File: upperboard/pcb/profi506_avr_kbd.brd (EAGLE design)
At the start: 22.8 x 53 mm, 15 parts, among them IC1 ATMEGA328-QFP32, IC2 DIP40 socket, Q1 16MHz

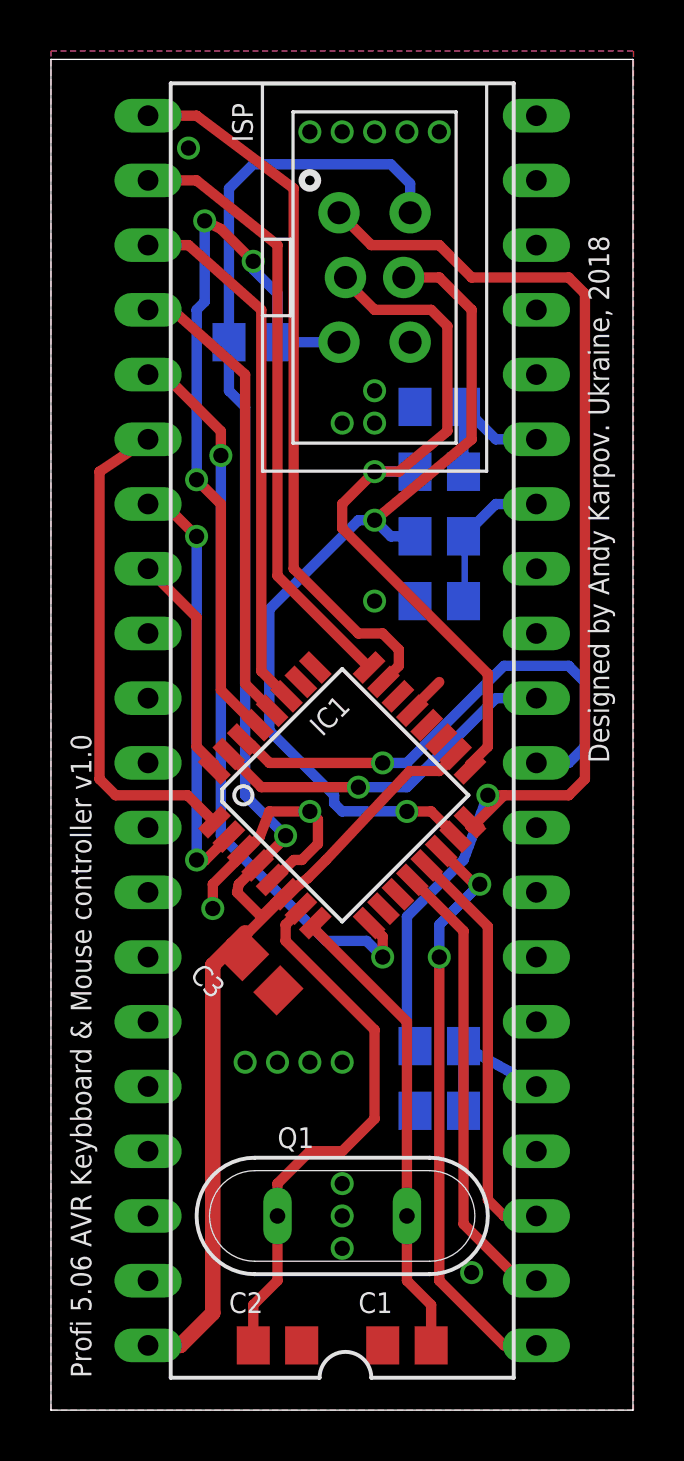
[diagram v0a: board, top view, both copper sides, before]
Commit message: new pcb v1.1 for avr kbd controller, added CS signal, added leds to indicate power status and activity
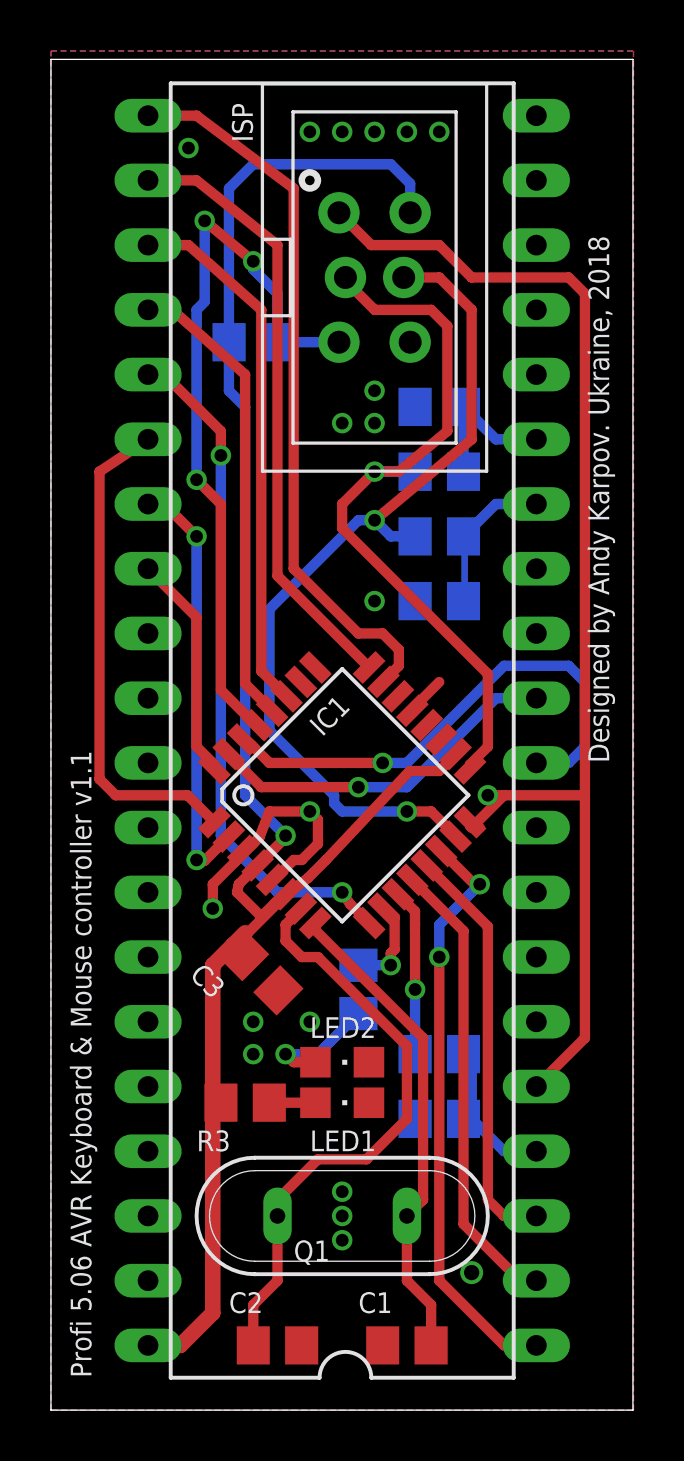
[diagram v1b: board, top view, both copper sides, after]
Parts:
- added LED1: PWR, adafruit:CHIPLED_0805
- added LED2: BUSY, adafruit:CHIPLED_0805
- added R8: 100, rcl:R0805
- added R9: 200, rcl:R0805
- R3: value 100 -> 470
- R4: value 200 -> 470
- moved R3 7.94 mm to (7.62, 12.1), flipped to the top
- moved R4 5.72 mm to (12.1, 16.5), turned to 90 degrees
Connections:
- net AVR_CLK renamed AVR_MOSI
- net AVR_DAT renamed AVR_SCK
- removed net AVR_RST: IC2.5, R3.2, R4.2
- new net AVR_BUSY: IC1.10, R4.2
- new net AVR_SS: IC2.4, R8.2, R9.2
- new net N$3: IC1.11, R8.1
- new net N$4: LED1.A, R3.1
- new net N$5: LED2.A, R4.1
- net GND: now also LED1.C, LED2.C, R9.1; no longer R4.1
- net MISO: now also IC2.5; no longer R3.1
- net VCC: now also R3.2
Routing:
- net N$3: track 0.00 -> 6.55 mm, vias 0 -> 1
- net AVR_SS: track 0.00 -> 6.25 mm
- net AVR_RST: track 5.81 -> 0.00 mm
- net N$5: track 0.00 -> 4.82 mm, vias 0 -> 1
- net AVR_BUSY: track 0.00 -> 3.90 mm, vias 0 -> 1
- net DATM: track 29.5 -> 26.9 mm
- net N$4: track 0.00 -> 1.81 mm
- net N$1: track 21.9 -> 23.7 mm
- net MISO: track 47.6 -> 49.1 mm
- net VCC: track 71.3 -> 72.0 mm
- net N$2: track 18.5 -> 19.0 mm
- net GND: vias 20 -> 19
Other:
- board text added: "Profi 5.06 AVR Keyboard & Mouse controller v1.1"
- board text removed: "Profi 5.06 AVR Keybboard & Mouse controller v1.0"
